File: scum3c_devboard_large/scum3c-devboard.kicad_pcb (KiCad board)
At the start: 2 copper layers, 39 x 69.3 mm, 59 parts, among them J1 CONSMA001-SMD-G-T, J10 Conn_01x02, J11 Conn_01x01, J2 47346-0001, J3 Conn_02x06_Odd_Even, J4 Conn_01x22, J5 Conn_02x04_Odd_Even, J6 Conn_01x03, J7 Conn_01x03, J8 Conn_01x03, J9 Conn_02x03_Odd_Even, U1 Perfboard, U10 74AVCH4T245D,118, U11 74AVCH4T245D,118, U12 S-85S1AB18-I6T1U, U13 74AVCH4T245D,118, U2 FT231XS-U, U3 74AVC1T45GS,132, U4 74AVC1T45GS,132, U5 ICM-20948, U6 S-85S1AB10-I6T1U, U7 S-85S1AB15-I6T1U, U8 scum3, U9 74AVCH4T245D,118

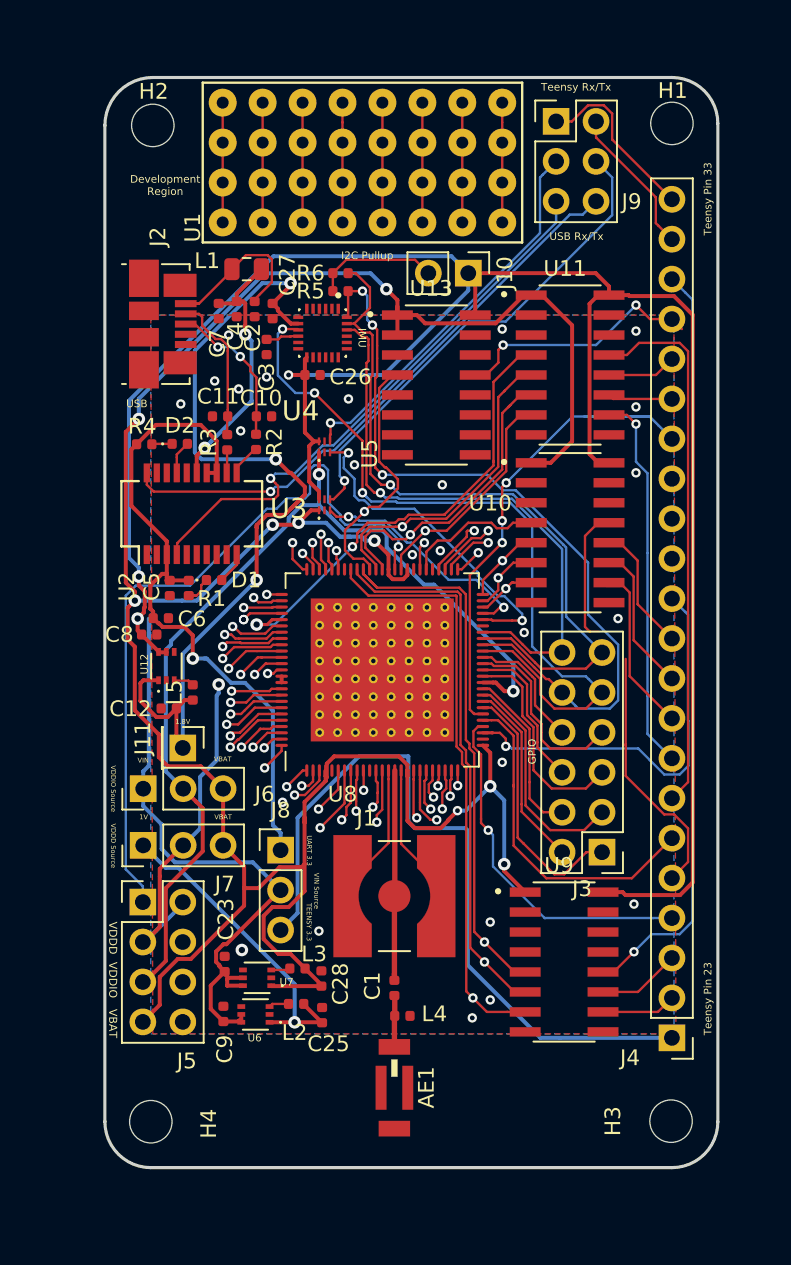
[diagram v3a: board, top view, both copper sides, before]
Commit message: Added images
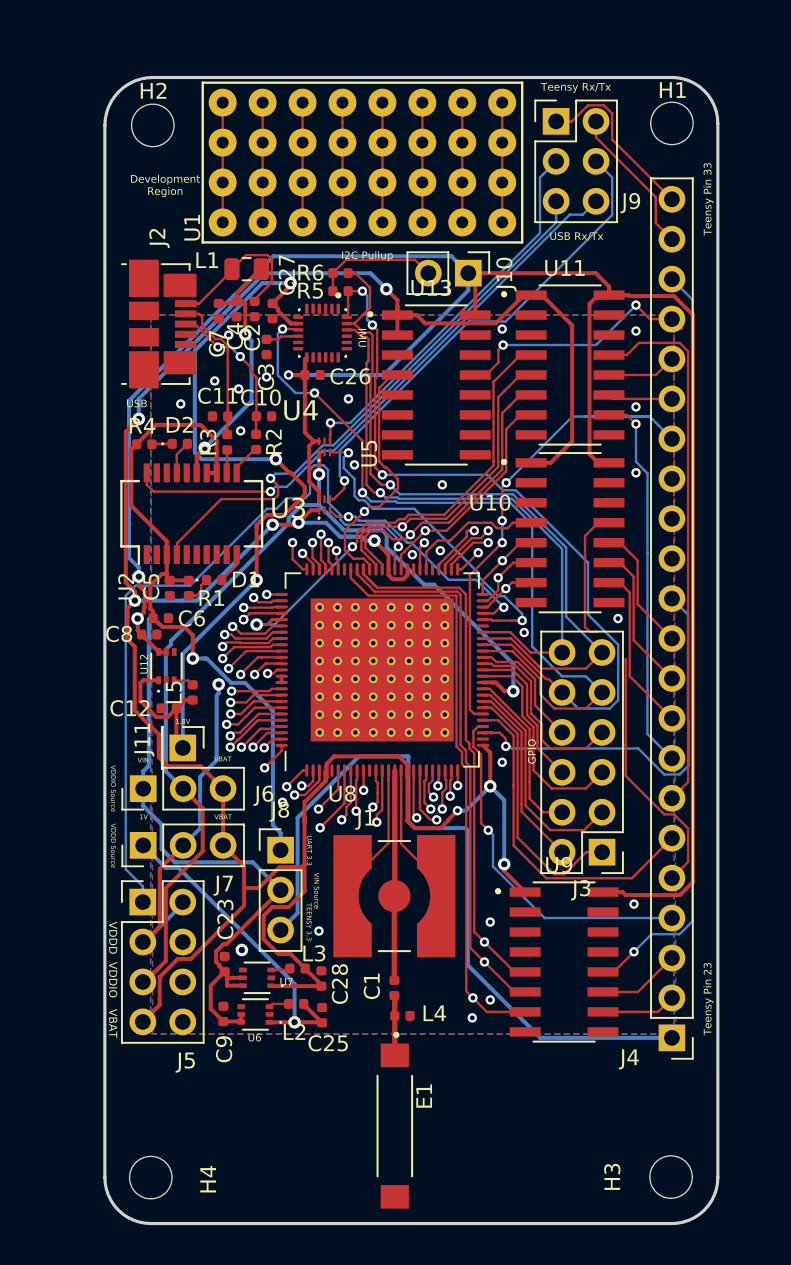
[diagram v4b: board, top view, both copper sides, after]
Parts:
- removed AE1: 2450AT42B100E, downloaded_libs:XCVR_2450AT42B100E
- added E1: 2450AT45A100E, downloaded_libs:ANT_2450AT45A100E, F.Cu at (212.5, 134.0)
- U3, U4: footprint SamacSys_Parts:74LVC1G3157GS132 -> downloaded_libs:74LVC1G3157GS132
- moved H3 3.56 mm to (230.1, 137.3)
- moved H4 3.56 mm to (197.0, 137.3)
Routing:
- net Net-(C1-Pad1): track 2.89 -> 3.81 mm
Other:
- board size 39 x 69.3 mm -> 39 x 72.9 mm

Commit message: With through-hole antenna
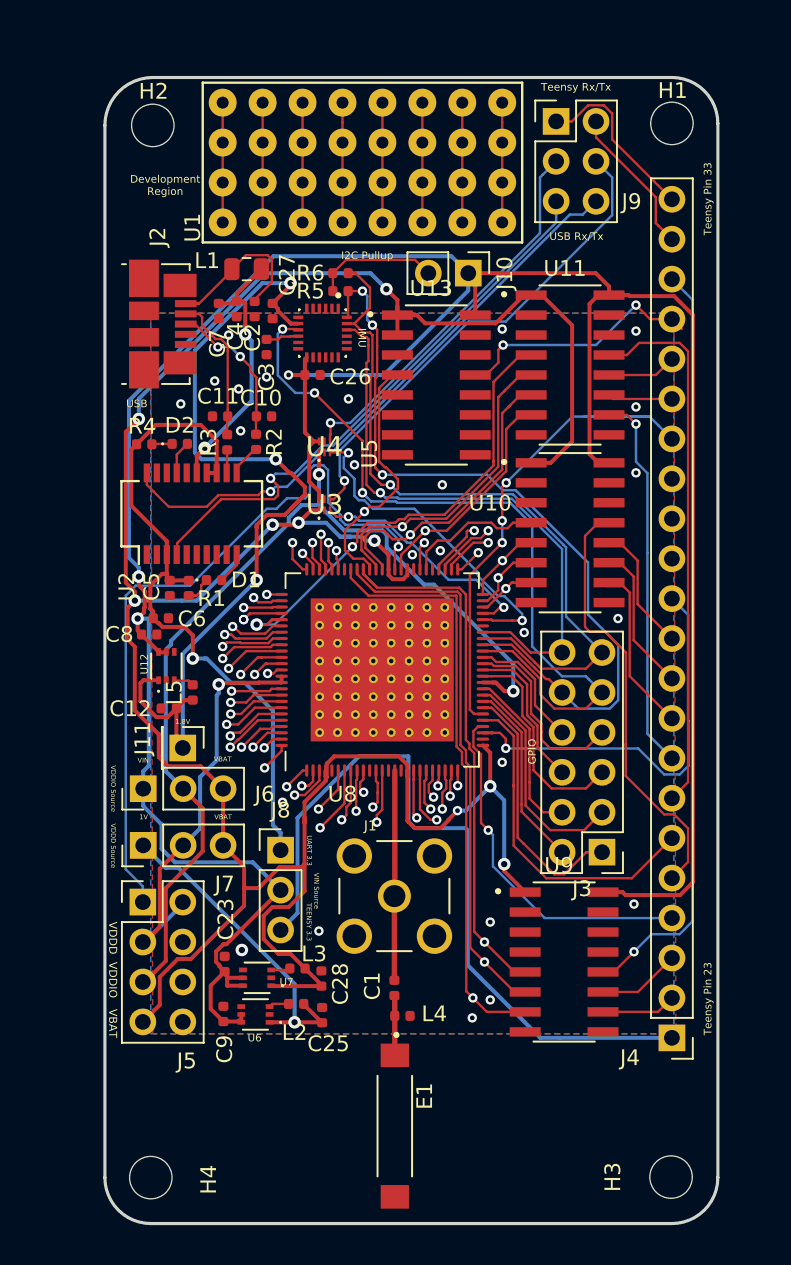
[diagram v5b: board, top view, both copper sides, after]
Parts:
- J1: value CONSMA001-SMD-G-T -> CONSMA001-G; footprint downloaded_libs:LINX_CONSMA001-SMD-G-T -> downloaded_libs:LINX_CONSMA001-G
- U3, U4: value 74AVC1T45GS,132 -> 74AVC1T45GS-Q100H; footprint downloaded_libs:74LVC1G3157GS132 -> SamacSys_Parts:74LVC1G3157GS132
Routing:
- net GND: track 18.8 -> 0.60 mm
- net +VDDD: track 22.7 -> 26.7 mm
- net /Teensy Connections/Clock33: track 25.1 -> 27.8 mm
- net /UART/RsRx33USB: track 37.2 -> 38.0 mm
- net +VIN: track 182.6 -> 183.3 mm

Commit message: Suggested changes
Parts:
- removed R5, R6: 10k, Resistor_SMD:R_0402_1005Metric
- added J12: Conn_02x01, Connector_PinHeader_2.54mm:PinHeader_2x01_P2.54mm_Vertical, F.Cu at (193.0, 103.5)
- added J13: Conn_02x01, Connector_PinHeader_2.54mm:PinHeader_2x01_P2.54mm_Vertical, F.Cu at (201.3, 116.2)
- added J14: Conn_01x01_Male, Connector_PinHeader_2.54mm:PinHeader_1x01_P2.54mm_Vertical, F.Cu at (220.5, 94.1)
- added J15: Conn_01x01_Male, Connector_PinHeader_2.54mm:PinHeader_1x01_P2.54mm_Vertical, F.Cu at (220.5, 97.8)
- added J16: Conn_02x01, Connector_PinHeader_2.54mm:PinHeader_2x01_P2.54mm_Vertical, F.Cu at (220.0, 120.5)
- added J17: Conn_02x01, Connector_PinHeader_2.54mm:PinHeader_2x01_P2.54mm_Vertical, F.Cu at (220.6, 113.9)
- J10: value Conn_01x02 -> Conn_02x01; footprint Connector_PinHeader_2.54mm:PinHeader_1x02_P2.54mm_Vertical -> Connector_PinHeader_2.54mm:PinHeader_2x01_P2.54mm_Vertical
- J4: footprint Connector_PinHeader_2.54mm:PinHeader_1x22_P2.54mm_Vertical -> SCUM:Teensy_Connector
- J5: value Conn_02x04_Odd_Even -> Conn_02x05_Odd_Even; footprint Connector_PinHeader_2.54mm:PinHeader_2x04_P2.54mm_Vertical -> Connector_PinHeader_2.54mm:PinHeader_2x05_P2.54mm_Vertical
- moved J4 53.5 mm to (232.7, 74.9), turned to 0 degrees
- moved J10 44.8 mm to (198.8, 120.7), turned to 0 degrees
- moved J5 5.23 mm to (191.8, 117.5)
- moved J7 5.12 mm to (192.0, 113.6)
- moved J6 5.12 mm to (192.0, 110.0)
- moved J11 5.12 mm to (194.6, 107.4)
- moved C2 5.08 mm to (198.5, 82.0)
- moved H2 4.57 mm to (192.5, 70.2)
- moved H4 4.57 mm to (192.4, 137.3)
- moved J2 4.12 mm to (193.6, 83.0)
- moved H1 2.54 mm to (232.7, 70.1)
- moved U9 2.54 mm to (225.8, 123.6)
- moved H3 2.54 mm to (232.6, 137.3)
- moved U10 2.54 mm to (226.2, 96.3)
- moved U11 2.54 mm to (226.2, 85.6)
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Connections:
- net /1Vin renamed +1VIN
- C28 pad 1: +VBAT -> +VBAT'
- J10 pad 1: +VIN -> +VBAT'
- J10 pad 2: Net-(J10-Pad2) -> +VBAT
- J5 pad 3: +VDDD -> +VDDD'
- J5 pad 5: +VDDIO -> +VDDIO'
- J5 pad 7: +VBAT -> +VBAT'
- J6 pad 2: +VDDIO -> +VDDIO'
- J6 pad 3: +VBAT -> +VBAT'
- J7 pad 2: +VDDD -> +VDDD'
- J7 pad 3: +VBAT -> +VBAT'
- L3 pad 1: +VBAT -> +VBAT'
- U1 pad 12: (no net) -> Net-(U1-Pad12)
- U1 pad 13: (no net) -> Net-(U1-Pad13)
- U1 pad 14: (no net) -> Net-(U1-Pad14)
- U1 pad 15: (no net) -> Net-(U1-Pad15)
- U1 pad 16: (no net) -> Net-(U1-Pad16)
- U1 pad 17: (no net) -> Net-(U1-Pad17)
- U1 pad 18: (no net) -> Net-(U1-Pad18)
- U1 pad 21: (no net) -> Net-(U1-Pad11)
- U1 pad 22: (no net) -> Net-(U1-Pad12)
- U1 pad 23: (no net) -> Net-(U1-Pad13)
- U1 pad 24: (no net) -> Net-(U1-Pad14)
- U1 pad 25: (no net) -> Net-(U1-Pad15)
- U1 pad 26: (no net) -> Net-(U1-Pad16)
- U1 pad 27: (no net) -> Net-(U1-Pad17)
- U1 pad 28: (no net) -> Net-(U1-Pad18)
- U1 pad 31: (no net) -> Net-(U1-Pad11)
- U1 pad 32: (no net) -> Net-(U1-Pad12)
- U1 pad 33: (no net) -> Net-(U1-Pad13)
- U1 pad 34: (no net) -> Net-(U1-Pad14)
- U1 pad 35: (no net) -> Net-(U1-Pad15)
- U1 pad 36: (no net) -> Net-(U1-Pad16)
- U1 pad 37: (no net) -> Net-(U1-Pad17)
- U1 pad 38: (no net) -> Net-(U1-Pad18)
- U1 pad 41: (no net) -> Net-(U1-Pad11)
- U1 pad 42: (no net) -> Net-(U1-Pad12)
- U1 pad 43: (no net) -> Net-(U1-Pad13)
- U1 pad 44: (no net) -> Net-(U1-Pad14)
- U1 pad 45: (no net) -> Net-(U1-Pad15)
- U1 pad 46: (no net) -> Net-(U1-Pad16)
- U1 pad 47: (no net) -> Net-(U1-Pad17)
- U1 pad 48: (no net) -> Net-(U1-Pad18)
- U4 pad 5: GND -> +VDDIO
- U5 pad 14: Net-(U5-Pad1) -> Net-(U5-Pad14)
- U5 pad 15: Net-(U5-Pad1) -> Net-(U5-Pad15)
- U5 pad 16: Net-(U5-Pad1) -> Net-(U5-Pad16)
- U5 pad 17: Net-(U5-Pad1) -> Net-(U5-Pad17)
- U5 pad 2: Net-(U5-Pad1) -> Net-(U5-Pad2)
- U5 pad 24: /GPIO13 -> /GPIO12
- U5 pad 3: Net-(U5-Pad1) -> Net-(U5-Pad3)
- U5 pad 4: Net-(U5-Pad1) -> Net-(U5-Pad4)
- U5 pad 5: Net-(U5-Pad1) -> Net-(U5-Pad5)
- U5 pad 6: Net-(U5-Pad1) -> Net-(U5-Pad6)
- U5 pad 9: /GPIO12 -> /GPIO13
- U7 pad 1: +VBAT -> +VBAT'
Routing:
- net (no net): track 61.0 -> 0.00 mm
- net +VBAT': track 0.00 -> 55.5 mm
- net +VIN: track 183.3 -> 206.4 mm, vias 3 -> 6
- net +VDDIO': track 0.00 -> 22.4 mm
- net /GPIO8: track 13.7 -> 30.8 mm, vias 0 -> 1
- net +VBAT: track 173.4 -> 157.6 mm, vias 9 -> 8
- net +VDDD': track 0.00 -> 15.3 mm
- net /GPIO9: track 9.71 -> 18.6 mm, vias 0 -> 1
- net +VDDIO: track 62.0 -> 53.5 mm
- net Net-(J10-Pad2): track 7.92 -> 0.00 mm
- net Net-(U1-Pad18): track 0.00 -> 7.62 mm
- net Net-(U1-Pad17): track 0.00 -> 7.62 mm
- net Net-(U1-Pad16): track 0.00 -> 7.62 mm
- net Net-(U1-Pad15): track 0.00 -> 7.62 mm
- net Net-(U1-Pad14): track 0.00 -> 7.62 mm
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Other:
- board size 39 x 72.9 mm -> 46.1 x 73.1 mm
- board text added: "IBAT"
- board text added: "IDDD"
- board text added: "IDDIO"
- board text added: "TEENSY"
- board text added: "TEXT THIS WAY"
- board text added: "Teensy Pin A9"
- board text added: "Teensy Pin TX5"
- board text added: "UART"
- board text added: "VDDD Select"
- board text added: "VDDIO Select"
- board text added: "VIN Select"
- board text removed: "1.8V"
- board text removed: "1V"
- board text removed: "I2C Pullup"
- board text removed: "TEENSY 3.3"
- board text removed: "Teensy Pin 23"
- board text removed: "Teensy Pin 33"
- board text removed: "UART 3.3"
- board text removed: "VDDD Source"
- board text removed: "VDDIO Source"
- board text removed: "VIN"
- board text removed: "VIN Source"
